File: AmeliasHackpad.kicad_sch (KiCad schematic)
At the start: 7 parts, among them SW1 SW_Push, SW2 SW_Push, SW3 SW_Push, SW4 SW_Push, U1 XIAO-RP2040-DIP

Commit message: Tried agian… restarted
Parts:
- added J1: Conn_01x04, Connector_PinHeader_2.54mm:PinHeader_1x04_P2.54mm_Vertical, symbol Connector_Generic:Conn_01x04
- U1: footprint Module:MOUDLE14P-XIAO-DIP-SMD -> OPL:XIAO-RP2040-DIP
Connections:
- net GND: no longer U1.13 (GND)
- net at U1.1 (GPIO26/ADC0/A0): now also J1.4 (Pin_4)
- net at U1.12 (3V3): now also J1.2 (Pin_2)
- net at U1.3 (GPIO28/ADC2/A2): now also J1.3 (Pin_3)
- new net: J1.1 (Pin_1), U1.13 (GND)
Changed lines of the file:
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@@
+	(wire
+		(pts
+			(xy 110.49 72.39) (xy 110.49 45.72)
+		)
+		(stroke
+			(width 0)
+			(type default)
+		)
+	)
+	(wire
+		(pts
+			(xy 151.13 50.8) (xy 135.89 50.8)
+		)
+		(stroke
+			(width 0)
+			(type default)
+		)
+	)
 	(wire
 		(pts
@@
 	(wire
 		(pts
+			(xy 71.12 87.63) (xy 72.39 87.63)
+		)
+		(stroke
+			(width 0)
+			(type default)
+		)
+	)
+	(wire
+		(pts
+			(xy 69.85 100.33) (xy 69.85 76.2)
+		)
+		(stroke
+			(width 0)
+			(type default)
+		)
+	)
+	(wire
+		(pts
 			(xy 107.95 80.01) (xy 113.03 80.01)
 		)
@@
 	(wire
 		(pts
+			(xy 69.85 76.2) (xy 72.39 76.2)
+		)
+		(stroke
+			(width 0)
+			(type default)
+		)
+	)
+	(wire
+		(pts
 			(xy 113.03 58.42) (xy 134.62 58.42)
 		)
@@
 	(wire
 		(pts
+			(xy 111.76 76.2) (xy 111.76 48.26)
+		)
+		(stroke
+			(width 0)
+			(type default)
+		)
+	)
+	(wire
+		(pts
 			(xy 129.54 63.5) (xy 129.54 68.58)
 		)
@@
 	(wire
 		(pts
+			(xy 118.11 99.06) (xy 118.11 101.6)
+		)
+		(stroke
+			(width 0)
+			(type default)
+		)
+	)
+	(wire
+		(pts
+			(xy 69.85 68.58) (xy 72.39 68.58)
+		)
+		(stroke
+			(width 0)
+			(type default)
+		)
+	)
+	(wire
+		(pts
 			(xy 115.57 87.63) (xy 115.57 62.23)
 		)
@@
 	(wire
 		(pts
-			(xy 118.11 99.06) (xy 118.11 106.68)
+			(xy 151.13 53.34) (xy 104.14 53.34)
 		)
 		(stroke
@@
 	(wire
 		(pts
+			(xy 69.85 62.23) (xy 69.85 68.58)
+		)
+		(stroke
+			(width 0)
+			(type default)
+		)
+	)
+	(wire
+		(pts
+			(xy 104.14 53.34) (xy 104.14 62.23)
+		)
+		(stroke
+			(width 0)
+			(type default)
+		)
+	)
+	(wire
+		(pts
 			(xy 107.95 91.44) (xy 116.84 91.44)
 		)
@@
 	(wire
 		(pts
+			(xy 135.89 50.8) (xy 135.89 100.33)
+		)
+		(stroke
+			(width 0)
+			(type default)
+		)
+	)
+	(wire
+		(pts
+			(xy 110.49 45.72) (xy 151.13 45.72)
+		)
+		(stroke
+			(width 0)
+			(type default)
+		)
+	)
+	(wire
+		(pts
 			(xy 107.95 83.82) (xy 114.3 83.82)
 		)
@@
 	(wire
 		(pts
+			(xy 69.85 100.33) (xy 135.89 100.33)
+		)
+		(stroke
+			(width 0)
+			(type default)
+		)
+	)
+	(wire
+		(pts
+			(xy 111.76 48.26) (xy 151.13 48.26)
+		)
+		(stroke
+			(width 0)
+			(type default)
+		)
+	)
+	(wire
+		(pts
 			(xy 128.27 68.58) (xy 129.54 68.58)
 		)
@@
 	(wire
 		(pts
+			(xy 107.95 76.2) (xy 111.76 76.2)
+		)
+		(stroke
+			(width 0)
+			(type default)
+		)
+	)
+	(wire
+		(pts
+			(xy 107.95 72.39) (xy 110.49 72.39)
+		)
+		(stroke
+			(width 0)
+			(type default)
+		)
+	)
+	(wire
+		(pts
 			(xy 134.62 58.42) (xy 134.62 99.06)
 		)
@@
 		(pts
 			(xy 116.84 63.5) (xy 129.54 63.5)
+		)
+		(stroke
+			(width 0)
+			(type default)
+		)
+	)
+	(wire
+		(pts
+			(xy 104.14 62.23) (xy 69.85 62.23)
 		)
 		(stroke
@@
 		(on_board yes)
 		(dnp no)
-		(fields_autoplaced yes)
 		(property "Reference" "#PWR03"
 			(at 104.14 68.58 0)
@@
 		)
 		(property "Value" "+5V"
-			(at 111.76 68.5799 90)
+			(at 105.156 64.516 90)
 			(effects
 				(font
@@
 			)
 		)
-		(property "Footprint" "Module:MOUDLE14P-XIAO-DIP-SMD"
+		(property "Footprint" "OPL:XIAO-RP2040-DIP"
 			(at 90.678 95.758 0)
 			(effects
@@
 	)
 	(symbol
-		(lib_id "power:GND")
-		(at 107.95 72.39 90)
-		(unit 1)
-		(exclude_from_sim no)
-		(in_bom yes)
-		(on_board yes)
-		(dnp no)
-		(fields_autoplaced yes)
-		(property "Reference" "#PWR02"
-			(at 114.3 72.39 0)
-			(effects
-				(font
-					(size 1.27 1.27)
-				)
-				(hide yes)
-			)
-		)
-		(property "Value" "GND"
-			(at 111.76 72.3899 90)
-			(effects
-				(font
-					(size 1.27 1.27)
-				)
-				(justify right)
-			)
-		)
-		(property "Footprint" ""
-			(at 107.95 72.39 0)
-			(effects
-				(font
-					(size 1.27 1.27)
-				)
-				(hide yes)
-			)
-		)
-		(property "Datasheet" ""
-			(at 107.95 72.39 0)
-			(effects
-				(font
-					(size 1.27 1.27)
-				)
-				(hide yes)
-			)
-		)
-		(property "Description" "Power symbol creates a global label with name \"GND\" , ground"
-			(at 107.95 72.39 0)
-			(effects
-				(font
-					(size 1.27 1.27)
-				)
-				(hide yes)
-			)
-		)
-		(pin "1"
-		)
-		(instances
-			(project ""
-				(path "/63dd5f8a-2016-4315-adee-55dd1b4905a7"
-					(reference "#PWR02")
-					(unit 1)
-				)
-			)
-		)
-	)
-	(symbol
 		(lib_id "Switch:SW_Push")
 		(at 123.19 88.9 0)
@@
 	(symbol
 		(lib_id "power:GND")
-		(at 118.11 106.68 0)
+		(at 118.11 101.6 0)
 		(unit 1)
 		(exclude_from_sim no)
@@
 		(fields_autoplaced yes)
 		(property "Reference" "#PWR01"
-			(at 118.11 113.03 0)
+			(at 118.11 107.95 0)
 			(effects
 				(font
@@
 		)
 		(property "Value" "GND"
-			(at 118.11 111.76 0)
+			(at 118.11 106.68 0)
 			(effects
 				(font
@@
 		)
 		(property "Footprint" ""
-			(at 118.11 106.68 0)
+			(at 118.11 101.6 0)
 			(effects
 				(font
@@
 		)
 		(property "Datasheet" ""
-			(at 118.11 106.68 0)
+			(at 118.11 101.6 0)
 			(effects
 				(font
@@
 		)
 		(property "Description" "Power symbol creates a global label with name \"GND\" , ground"
-			(at 118.11 106.68 0)
+			(at 118.11 101.6 0)
 			(effects
 				(font
@@
 					(unit 1)
 				)
+			)
+		)
+	)
+	(symbol
+		(lib_id "Connector_Generic:Conn_01x04")
+		(at 156.21 48.26 0)
+		(unit 1)
+		(exclude_from_sim no)
+		(in_bom yes)
+		(on_board yes)
+		(dnp no)
+		(fields_autoplaced yes)
+		(property "Reference" "J1"
+			(at 158.75 48.2599 0)
+			(effects
+				(font
+					(size 1.27 1.27)
+				)
+				(justify left)
+			)
+		)
+		(property "Value" "Conn_01x04"
+			(at 158.75 50.7999 0)
+			(effects
+				(font
+					(size 1.27 1.27)
+				)
+				(justify left)
+			)
+		)
+		(property "Footprint" "Connector_PinHeader_2.54mm:PinHeader_1x04_P2.54mm_Vertical"
+			(at 156.21 48.26 0)
+			(effects
+				(font
+					(size 1.27 1.27)
+				)
+				(hide yes)
+			)
+		)
+		(property "Datasheet" "~"
+			(at 156.21 48.26 0)
+			(effects
+				(font
+					(size 1.27 1.27)
+				)
+				(hide yes)
+			)
+		)
+		(property "Description" "Generic connector, single row, 01x04, script generated (kicad-library-utils/schlib/autogen/connector/)"
+			(at 156.21 48.26 0)
+			(effects
+				(font
+					(size 1.27 1.27)
+				)
+				(hide yes)
+			)
+		)
+		(pin "1"
+		)
+		(pin "2"
+		)
+		(pin "3"
+		)
+		(pin "4"
+		)
+		(instances
+			(project ""
+				(path "/63dd5f8a-2016-4315-adee-55dd1b4905a7"
+					(reference "J1")
+					(unit 1)
+				)

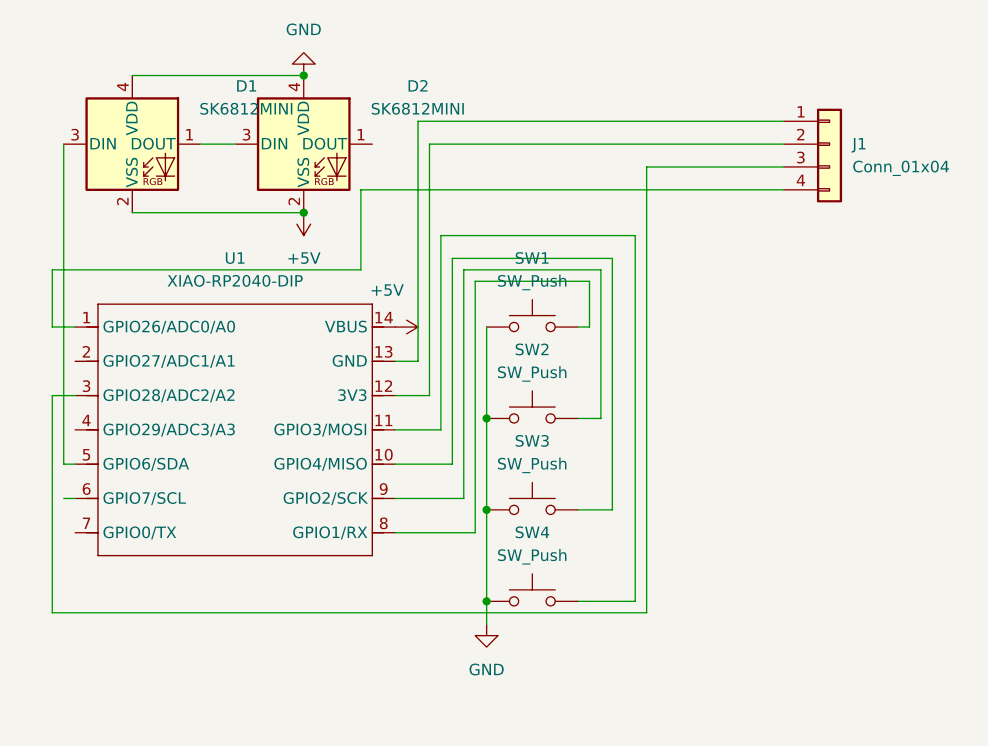
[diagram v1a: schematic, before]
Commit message: Updated Macropad and added a rotary encoder
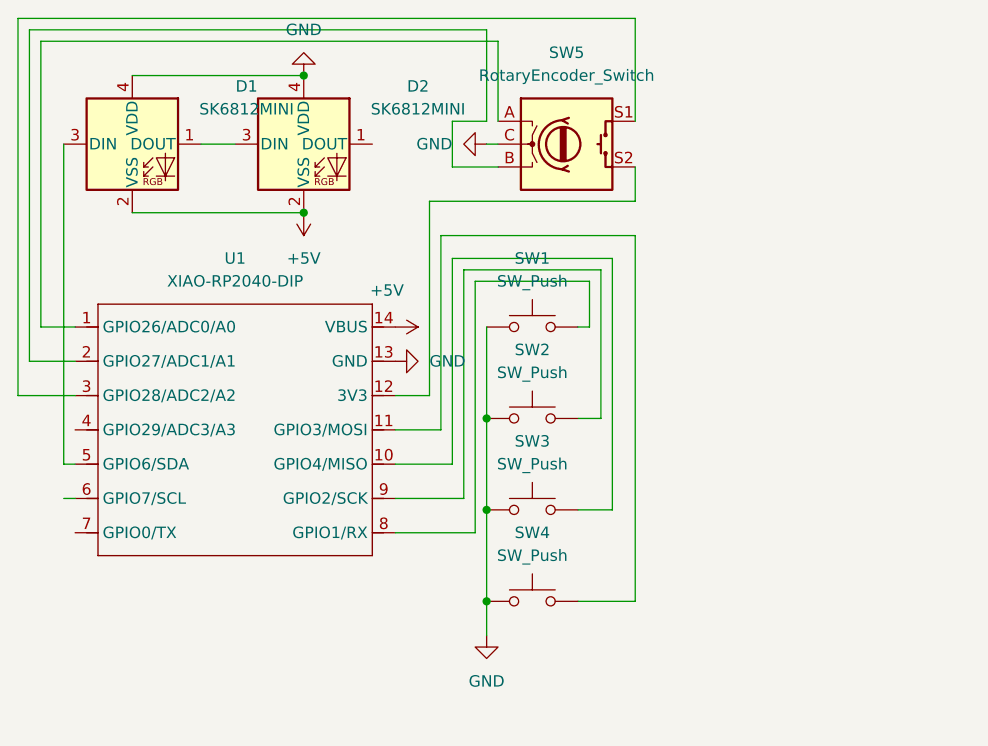
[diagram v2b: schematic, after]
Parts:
- removed J1: Conn_01x04, Connector_PinHeader_2.54mm:PinHeader_1x04_P2.54mm_Vertical, symbol Connector_Generic:Conn_01x04
- added SW5: RotaryEncoder_Switch, Rotary_Encoder:RotaryEncoder_Alps_EC11E-Switch_Vertical_H20mm, symbol Device:RotaryEncoder_Switch
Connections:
- net GND: now also U1.13 (GND), SW5.C
- net at U1.1 (GPIO26/ADC0/A0): now also SW5.A
- net at U1.12 (3V3): now also SW5.S2
- net at U1.2 (GPIO27/ADC1/A1): now also SW5.B
- net at U1.3 (GPIO28/ADC2/A2): now also SW5.S1
